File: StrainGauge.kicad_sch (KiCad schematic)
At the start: 20 parts, among them J1 Conn_01x04, J2 Conn_01x04, U1 INA333xxDGK, U2 REF2025

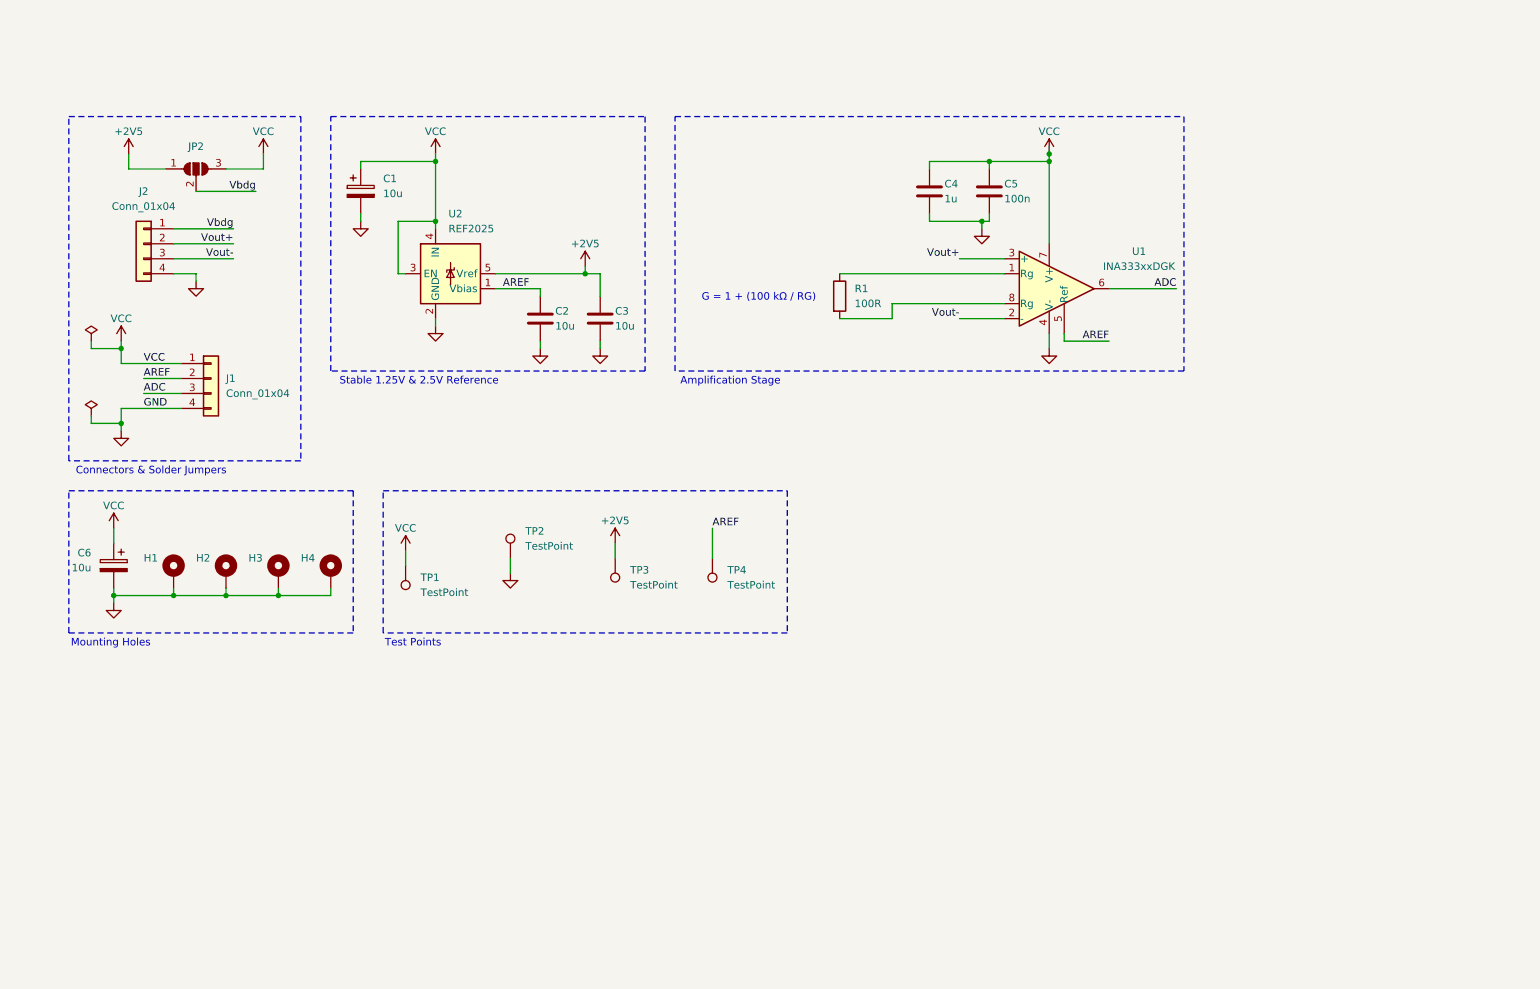
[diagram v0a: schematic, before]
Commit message: added limiting resistor + calculation
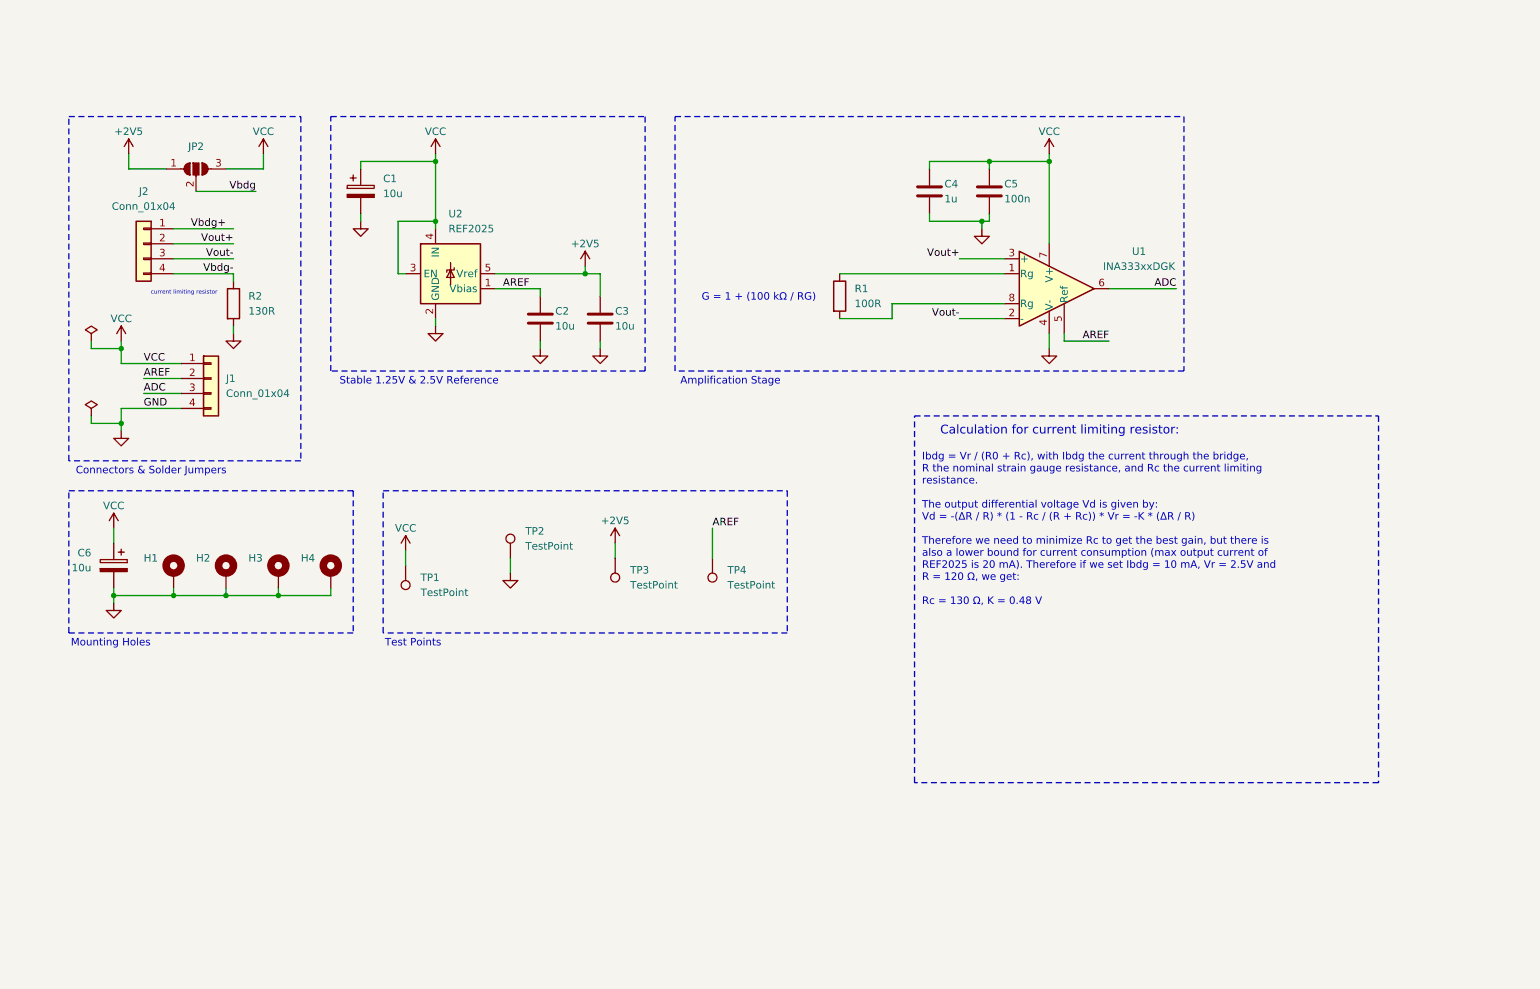
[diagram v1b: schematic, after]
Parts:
- added R2: 130R, symbol Device:R
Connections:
- net GND: now also R2.2; no longer J2.4 (Pin_4)
- net Vbdg: no longer J2.1 (Pin_1)
- new net Vbdg+: J2.1 (Pin_1)
- new net Vbdg-: J2.4 (Pin_4), R2.1
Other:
- note added: "Calculation for current limiting resistor:"
- note added: "Ibdg = Vr / (R0 + Rc), with Ibdg the current through the bridge, R the nominal strain gauge resistance, and Rc the current limiting resistance. The output differential voltage Vd is given by: Vd = -(ΔR / R) * (1 - Rc / (R + Rc)) * Vr = -K * (ΔR / R) Therefore we need to minimize Rc to get the best gain, but there is also a lower bound for current consumption (max output current of REF2025 is 20 m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"
- note added: "current limiting resistor"
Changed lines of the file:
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@@
+	)
+	(junction
+		(at 199.39 53.34)
+		(diameter 0)
+		(color 0 0 0 0)
 	)
 	(junction
@@
 	)
 	(junction
-		(at 199.39 53.34)
-		(diameter 0)
-		(color 0 0 0 0)
-	)
-	(junction
 		(at 40.64 127)
 		(diameter 0)
@@
 		(color 0 0 0 0)
 	)
-	(junction
-		(at 199.39 52.07)
-		(diameter 0)
-		(color 0 0 0 0)
-	)
 	(wire
 		(pts
@@
 	(wire
 		(pts
+			(xy 60.96 72.39) (xy 60.96 73.66)
+		)
+		(stroke
+			(width 0)
+			(type default)
+		)
+	)
+	(wire
+		(pts
 			(xy 95.25 63.5) (xy 95.25 64.77)
 		)
@@
 	(wire
 		(pts
-			(xy 54.61 73.66) (xy 54.61 72.39)
+			(xy 199.39 53.34) (xy 199.39 67.31)
 		)
 		(stroke
@@
 	(wire
 		(pts
-			(xy 199.39 53.34) (xy 189.23 53.34)
+			(xy 60.96 82.55) (xy 60.96 81.28)
 		)
 		(stroke
@@
 	(wire
 		(pts
-			(xy 199.39 53.34) (xy 199.39 67.31)
-		)
-		(stroke
-			(width 0)
-			(type default)
-		)
-	)
-	(wire
-		(pts
 			(xy 199.39 52.07) (xy 199.39 53.34)
 		)
@@
 	(wire
 		(pts
-			(xy 54.61 72.39) (xy 50.8 72.39)
+			(xy 189.23 53.34) (xy 199.39 53.34)
+		)
+		(stroke
+			(width 0)
+			(type default)
+		)
+	)
+	(wire
+		(pts
+			(xy 50.8 72.39) (xy 60.96 72.39)
 		)
 		(stroke
@@
 		(pts
 			(xy 163.83 80.01) (xy 172.72 80.01)
-		)
-		(stroke
-			(width 0)
-			(type default)
-		)
-	)
-	(wire
-		(pts
-			(xy 199.39 50.8) (xy 199.39 52.07)
 		)
 		(stroke
@@
 	)
 	(rectangle
+		(start 176.53 96.52)
+		(end 255.27 158.75)
+		(stroke
+			(width 0)
+			(type dash_dot)
+		)
+		(fill
+			(type none)
+		)
+	)
+	(rectangle
 		(start 33.02 109.22)
 		(end 81.28 133.35)
@@
 		)
 	)
+	(text "Ibdg = Vr / (R0 + Rc), with Ibdg the current through the bridge, \nR the nominal strain gauge resistance, and Rc the current limiting\nresistance.\n\nThe output differential voltage Vd is given by:\nVd = -(ΔR / R) * (1 - Rc / (R + Rc)) * Vr = -K * (ΔR / R)\n\nTherefore we need to minimize Rc to get the best gain, but there is\nalso a lower bound for current consumption (max output current of\nREF2025 is 20 mA). Therefore if we set Ibdg = 10 mA, Vr = 2.5V and\nR = 120 Ω, we get:\n\nRc = 130 Ω, K = 0.48 V"
+		(exclude_from_sim no)
+		(at 177.8 115.824 0)
+		(effects
+			(font
+				(size 1.27 1.27)
+				(color 0 0 0 1)
+			)
+			(justify left)
+		)
+	)
 	(text "Mounting Holes"
 		(exclude_from_sim no)
@@
 		)
 	)
+	(text "current limiting resistor"
+		(exclude_from_sim no)
+		(at 52.578 75.692 0)
+		(effects
+			(font
+				(size 0.7 0.7)
+			)
+		)
+	)
 	(text "G = 1 + (100 kΩ / RG) "
 		(exclude_from_sim no)
@@
 			(font
 				(size 1.27 1.27)
+			)
+		)
+	)
+	(text "Calculation for current limiting resistor:"
+		(exclude_from_sim no)
+		(at 201.168 99.06 0)
+		(effects
+			(font
+				(size 1.5 1.5)
 			)
 		)
@@
 		)
 	)
-	(label "Vbdg"
-		(at 60.96 64.77 180)
+	(label "Vbdg+"
+		(at 59.69 64.77 180)
 		(fields_autoplaced yes)
 		(effects
@@
 			)
 			(justify left bottom)
+		)
+	)
+	(label "Vbdg-"
+		(at 60.96 72.39 180)
+		(fields_autoplaced yes)
+		(effects
+			(font
+				(size 1.27 1.27)
+			)
+			(justify right bottom)
 		)
 	)
@@
 	)
 	(symbol
+		(lib_id "power:GND")
+		(at 60.96 82.55 0)
+		(unit 1)
+		(exclude_from_sim no)
+		(in_bom yes)
+		(on_board yes)
+		(dnp no)
+		(fields_autoplaced yes)
+		(property "Reference" "#PWR03"
+			(at 60.96 88.9 0)
+			(effects
+				(font
+					(size 1.27 1.27)
+				)
+				(hide yes)
+			)
+		)
+		(property "Value" "GND"
+			(at 60.96 87.63 0)
+			(effects
+				(font
+					(size 1.27 1.27)
+				)
+				(hide yes)
+			)
+		)
+		(property "Footprint" ""
+			(at 60.96 82.55 0)
+			(effects
+				(font
+					(size 1.27 1.27)
+				)
+				(hide yes)
+			)
+		)
+		(property "Datasheet" ""
+			(at 60.96 82.55 0)
+			(effects
+				(font
+					(size 1.27 1.27)
+				)
+				(hide yes)
+			)
+		)
+		(property "Description" "Power symbol creates a global label with name \"GND\" , ground"
+			(at 60.96 82.55 0)
+			(effects
+				(font
+					(size 1.27 1.27)
+				)
+				(hide yes)
+			)
+		)
+		(pin "1"
+		)
+		(instances
+			(project "StrainGauge"
+				(path "/1c58ffeb-c530-4561-bcfa-51e04fb88036"
+					(reference "#PWR03")
+					(unit 1)
+				)
+			)
+		)
+	)
+	(symbol
 		(lib_id "power:+2V5")
 		(at 120.65 71.12 0)
@@
 				(path "/1c58ffeb-c530-4561-bcfa-51e04fb88036"
 					(reference "#PWR018")
+					(unit 1)
+				)
+			)
+		)
+	)
+	(symbol
+		(lib_id "Device:R")
+		(at 60.96 77.47 0)
+		(unit 1)
+		(exclude_from_sim no)
+		(in_bom yes)
+		(on_board yes)
+		(dnp no)
+		(fields_autoplaced yes)
+		(property "Reference" "R2"
+			(at 63.5 76.1999 0)
+			(effects
+				(font
+					(size 1.27 1.27)
+				)
+				(justify left)
+			)
+		)
+		(property "Value" "130R"
+			(at 63.5 78.7399 0)
+			(effects
+				(font
+					(size 1.27 1.27)
+				)
+				(justify left)
+			)
+		)
+		(property "Footprint" ""
+			(at 59.182 77.47 90)
+			(effects
+				(font
+					(size 1.27 1.27)
+				)
+				(hide yes)
+			)
+		)
+		(property "Datasheet" "~"
+			(at 60.96 77.47 0)
+			(effects
+				(font
+					(size 1.27 1.27)
+				)
+				(hide yes)
+			)
+		)
+		(property "Description" "Resistor"
+			(at 60.96 77.47 0)
+			(effects
+				(font
+					(size 1.27 1.27)
+				)
+				(hide yes)
+			)
+		)
+		(pin "1"
+		)
+		(pin "2"
+		)
+		(instances
+			(project ""
+				(path "/1c58ffeb-c530-4561-bcfa-51e04fb88036"
+					(reference "R2")
 					(unit 1)
 				)
@@
 					(unit 1)
 				)
-			)
-		)
-	)
-	(symbol
-		(lib_id "power:GND")
-		(at 54.61 73.66 0)
-		(unit 1)
-		(exclude_from_sim no)
-		(in_bom yes)
-		(on_board yes)
-		(dnp no)
-		(fields_autoplaced yes)
-		(property "Reference" "#PWR03"
-			(at 54.61 80.01 0)
-			(effects
-				(font
-					(size 1.27 1.27)
-				)
-				(hide yes)
-			)
-		)
-		(property "Value" "GND"
-			(at 54.61 78.74 0)
-			(effects
-				(font
-					(size 1.27 1.27)
-				)
-				(hide yes)
-			)
-		)
-		(property "Footprint" ""
-			(at 54.61 73.66 0)
-			(effects
-				(font
-					(size 1.27 1.27)
-				)
-				(hide yes)
-			)
-		)
-		(property "Datasheet" ""
-			(at 54.61 73.66 0)
-			(effects
-				(font
-					(size 1.27 1.27)
-				)
-				(hide yes)
-			)
-		)
-		(property "Description" "Power symbol creates a global label with name \"GND\" , ground"
-			(at 54.61 73.66 0)
-			(effects
-				(font
-					(size 1.27 1.27)
-				)
-				(hide yes)
-			)
-		)
-		(pin "1"
-		)
-		(instances
-			(project "StrainGauge"
-				(path "/1c58ffeb-c530-4561-bcfa-51e04fb88036"
-					(reference "#PWR03")
-					(unit 1)
-				)

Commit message: added example schematic image of stable voltage source example
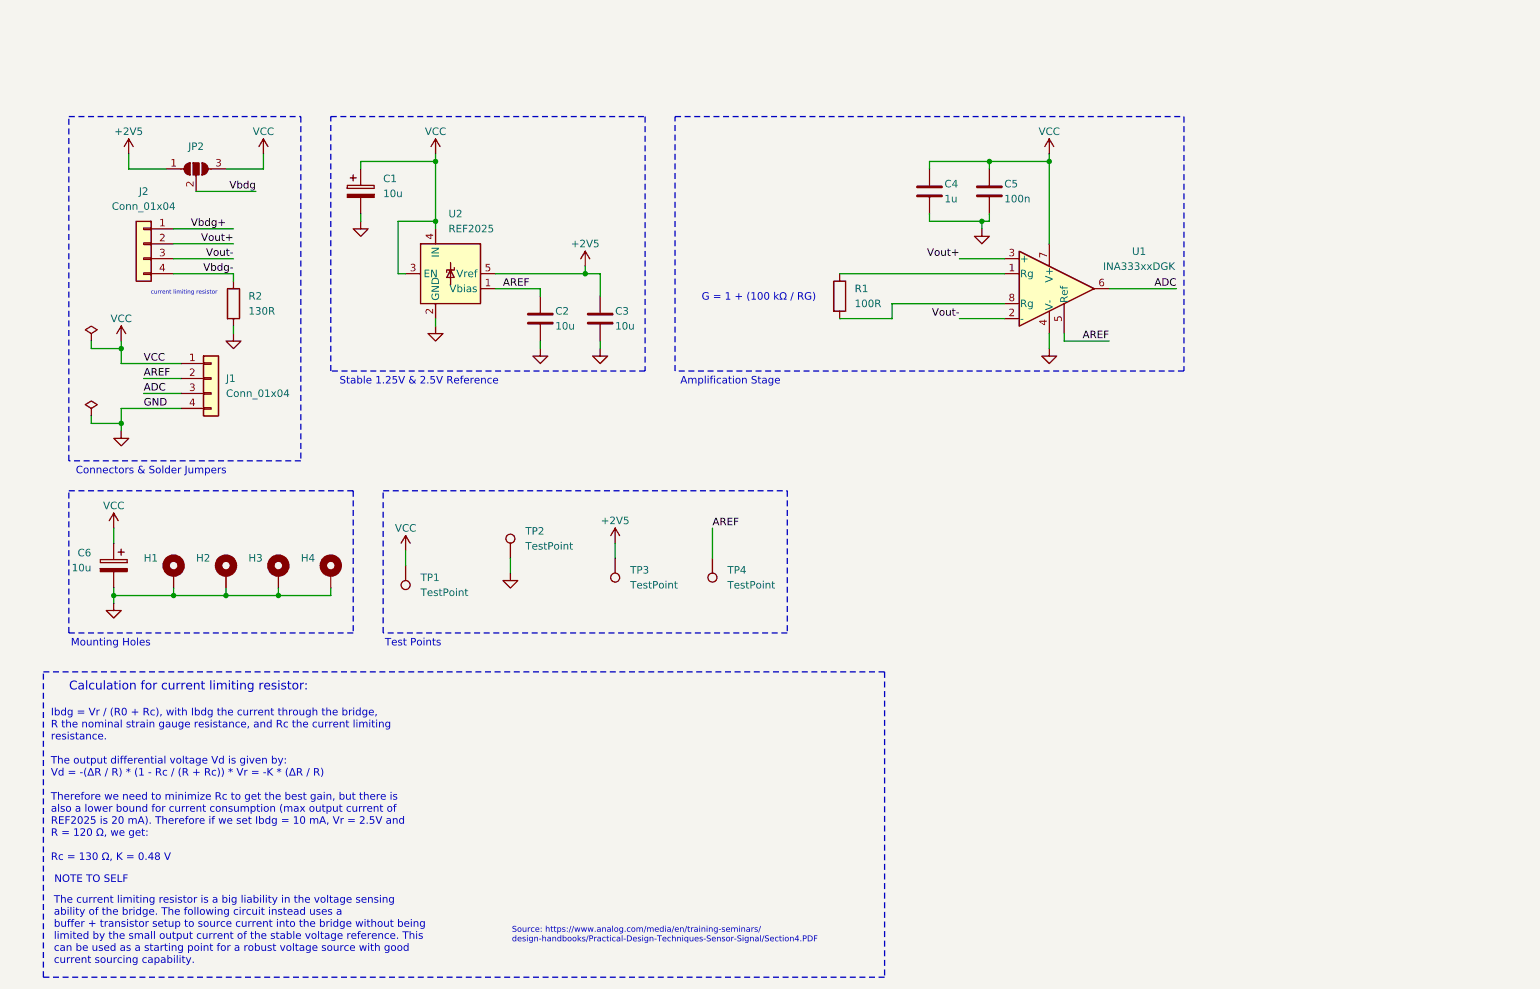
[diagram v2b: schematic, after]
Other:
- note added: "NOTE TO SELF"
- note added: "Source: https://www.analog.com/media/en/training-seminars/ design-handbooks/Practical-Design-Techniques-Sensor-Signal/Section4.PDF"
- note added: "The current limiting resistor is a big liability in the voltage sensing ability of the bridge. The following circuit instead uses a buffer + transistor setup to source current into the bridge without being limited by the small output current of the stable voltage reference. This can be used as a starting point for a robust voltage source with good current sourcing capability."

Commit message: added decoupling caps on input and power input of INA333
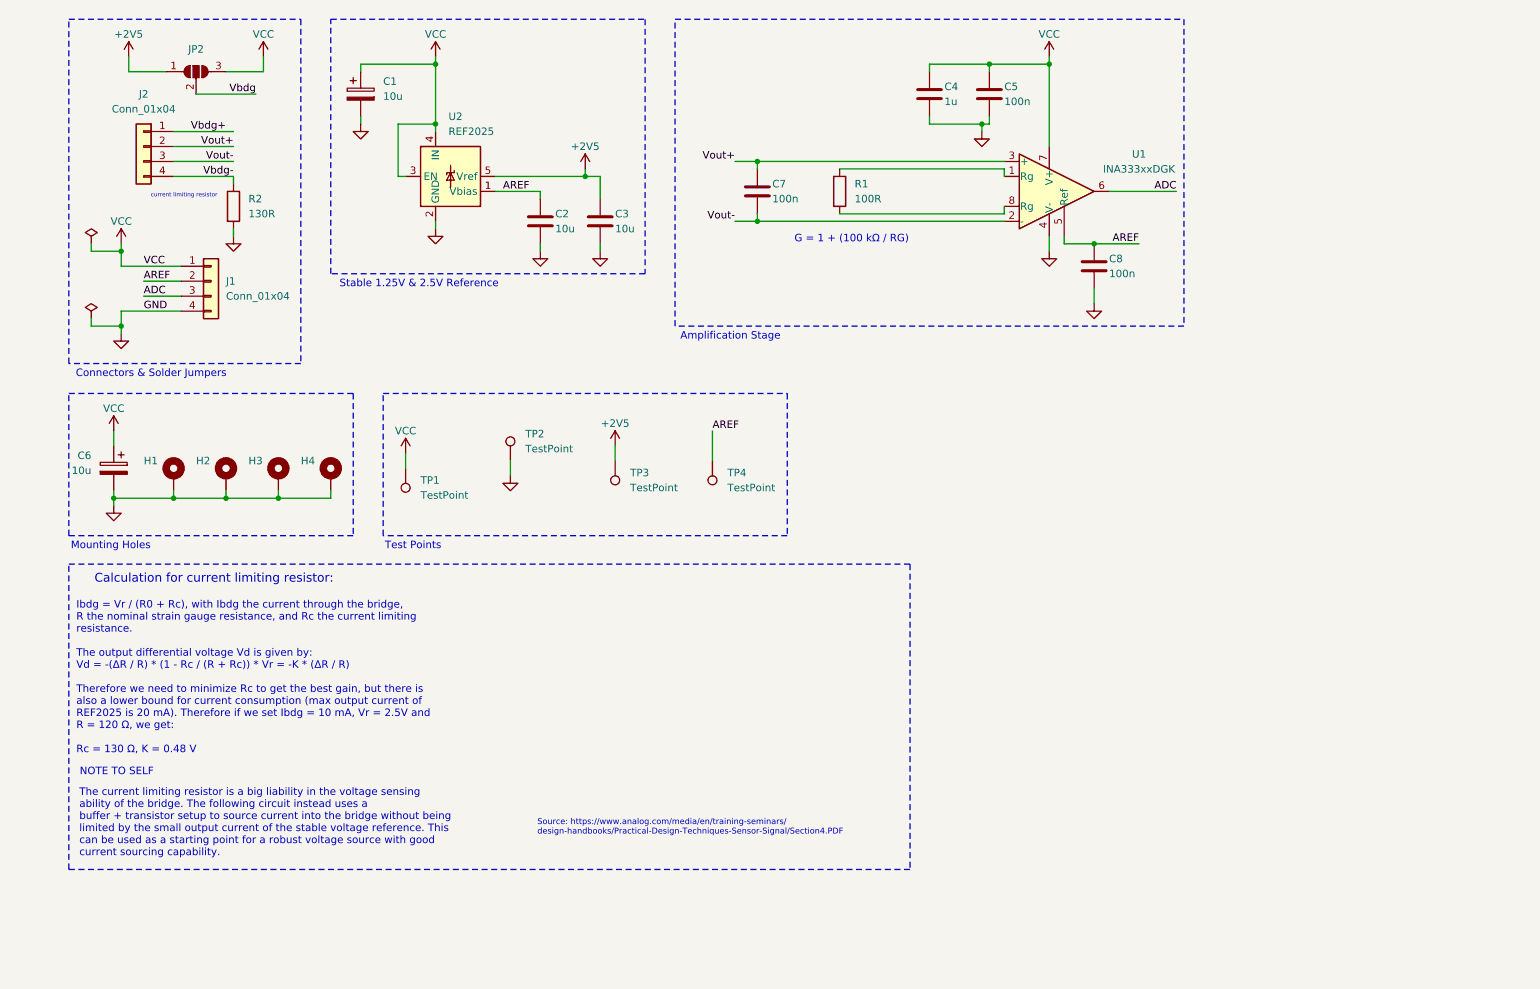
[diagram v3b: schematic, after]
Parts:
- added C7, C8: 100n, symbol Device:C
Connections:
- net AREF: now also C8.1
- net GND: now also C8.2
- net Vout+: now also C7.1
- net Vout-: now also C7.2
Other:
- moved on the sheet: C1, C2, C3, C4, C5, C6, H1, H2, H3, H4, J1, J2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
